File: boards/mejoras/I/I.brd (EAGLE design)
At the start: 100 x 45 mm, 5 parts

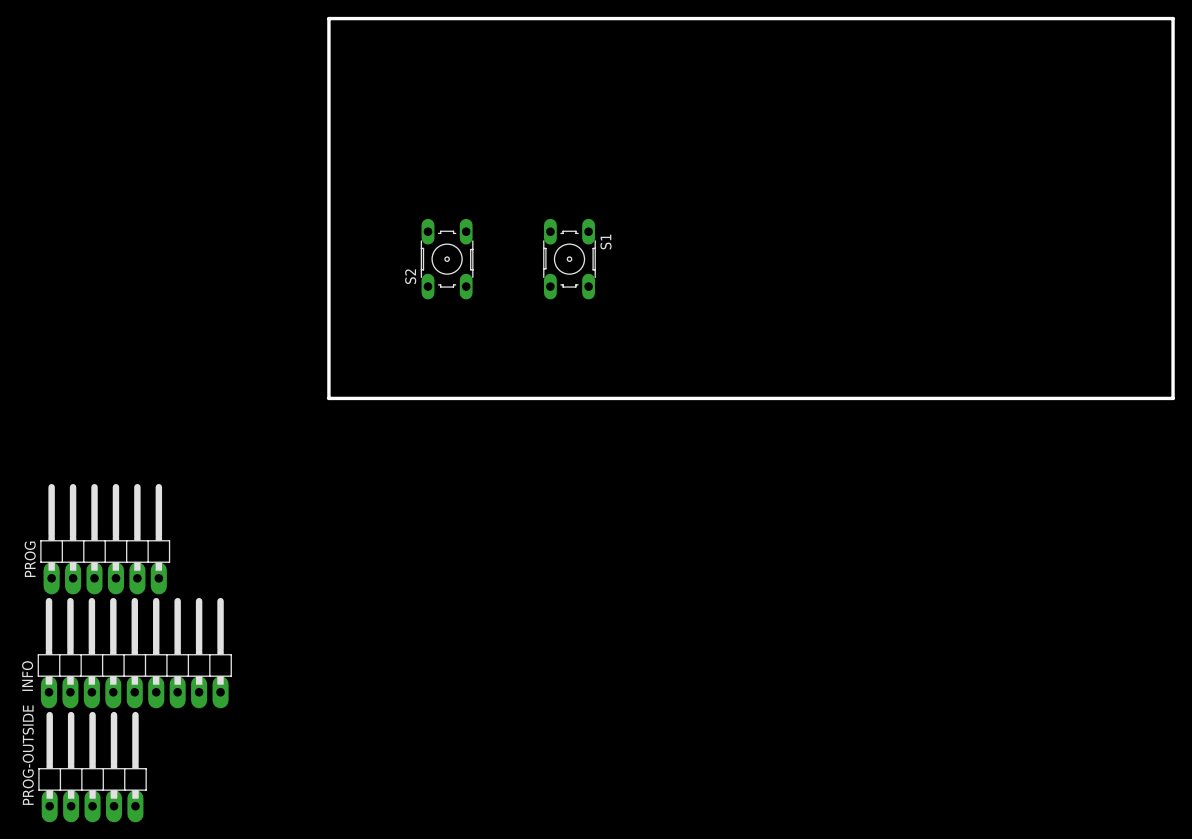
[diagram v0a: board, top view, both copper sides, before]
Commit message: added circuit H and I
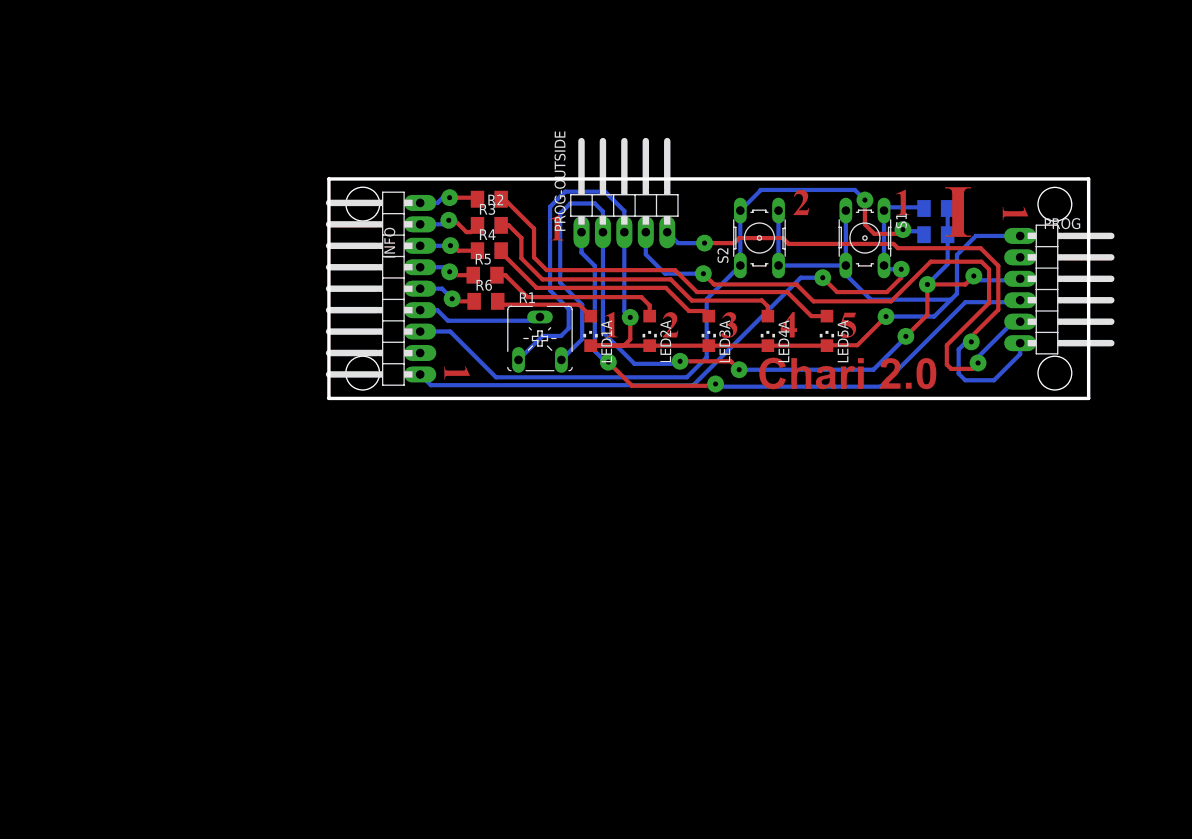
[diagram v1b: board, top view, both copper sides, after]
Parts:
- added LED1A, LED2A, LED3A, LED4A, LED5A: (no value), adafruit:CHIPLED_1206
- added R1: (no value), pot:CA6V
- added R2, R3, R4, R5, R6, R7, R8: (no value), rcl:M1206
- moved PROG 116.2 mm to (85.7, 12.9), turned to 270 degrees
- moved PROG-OUTSIDE 92.7 mm to (35.0, 23.5)
- moved INFO 53.3 mm to (7.00, 13.0), turned to 90 degrees
- moved S2 37.1 mm to (51.0, 19.0)
- moved S1 35.1 mm to (63.5, 19.0)
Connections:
- new net 5V: PROG-OUTSIDE.2, PROG.3, R1.E, R7.2, R8.2
- new net MCRL: PROG-OUTSIDE.1, PROG.4
- new net N$1: LED1A.A, R6.2
- new net N$10: INFO.5, R6.1
- new net N$11: INFO.4, R1.S
- new net N$2: LED2A.A, R5.2
- new net N$3: LED3A.A, R4.2
- new net N$4: LED4A.A, R3.2
- new net N$5: LED5A.A, R2.2
- new net N$6: INFO.9, R2.1
- new net N$7: INFO.8, R3.1
- new net N$8: INFO.7, R4.1
- new net N$9: INFO.6, R5.1
- new net PGC: PROG-OUTSIDE.5, PROG.6
- new net PGD: PROG-OUTSIDE.4, PROG.5
- net B1: now also INFO.1, R7.1
- net B2: now also INFO.3, R8.1
- net GND: now also LED1A.C, LED2A.C, LED3A.C, LED4A.C, LED5A.C, PROG-OUTSIDE.3, PROG.1, R1.A
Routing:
- net GND: track 0.00 -> 148.6 mm, vias 0 -> 2
- net 5V: track 0.00 -> 108.9 mm, vias 0 -> 5
- net B2: track 0.00 -> 83.3 mm, vias 0 -> 2
- net B1: track 0.00 -> 79.0 mm, vias 0 -> 2
- net PGD: track 0.00 -> 72.9 mm, vias 0 -> 2
- net MCRL: track 0.00 -> 71.5 mm, vias 0 -> 2
- net PGC: track 0.00 -> 66.6 mm, vias 0 -> 2
- net N$5: track 0.00 -> 46.3 mm
- net N$4: track 0.00 -> 38.8 mm
- net N$3: track 0.00 -> 27.9 mm
- net N$2: track 0.00 -> 20.8 mm
- net N$11: track 0.00 -> 14.9 mm
- net N$1: track 0.00 -> 11.7 mm
- net N$7: track 0.00 -> 7.90 mm, vias 0 -> 1
- net N$6: track 0.00 -> 7.85 mm, vias 0 -> 1
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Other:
- board size 100 x 45 mm -> 90 x 26 mm

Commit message: updated board h and i
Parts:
- moved R2 20.3 mm to (37.9, 16.2)
- moved R8 15.0 mm to (57.3, 23.0)
- moved R3 14.8 mm to (32.8, 15.2)
- moved R4 9.38 mm to (27.7, 14.0)
- moved PROG 6.00 mm to (79.7, 12.9)
- moved R5 3.18 mm to (21.6, 15.3)
- moved R6 3.13 mm to (21.6, 12.4)
- moved INFO 3.00 mm to (10.0, 13.0)
- moved R7 2.11 mm to (69.8, 22.3)
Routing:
- net N$5: track 46.3 -> 22.4 mm
- net N$6: track 7.85 -> 28.5 mm
- net B2: track 83.3 -> 62.9 mm, vias 2 -> 0
- net N$4: track 38.8 -> 21.4 mm
- net N$7: track 7.90 -> 21.4 mm
- net PGC: track 66.6 -> 53.2 mm
- net 5V: track 108.9 -> 122.2 mm, vias 5 -> 4
- net PGD: track 72.9 -> 62.3 mm
- net GND: track 148.6 -> 138.1 mm
- net N$3: track 27.9 -> 17.7 mm
- net B1: track 79.0 -> 69.1 mm
- net N$8: track 7.05 -> 14.9 mm
- net MCRL: track 71.5 -> 66.4 mm
- net N$11: track 14.9 -> 11.6 mm
- net N$1: track 11.7 -> 9.10 mm
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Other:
- board size 90 x 26 mm -> 80 x 26 mm

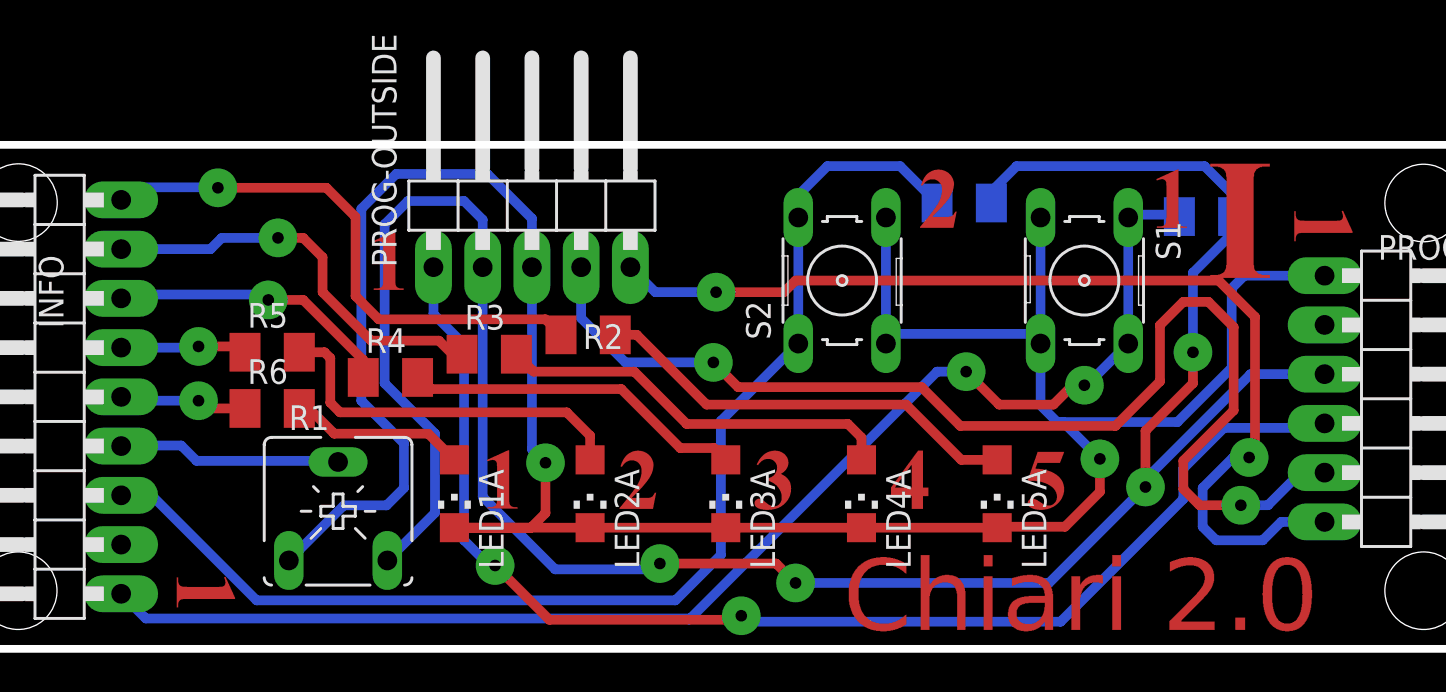
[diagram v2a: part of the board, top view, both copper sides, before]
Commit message: added on button
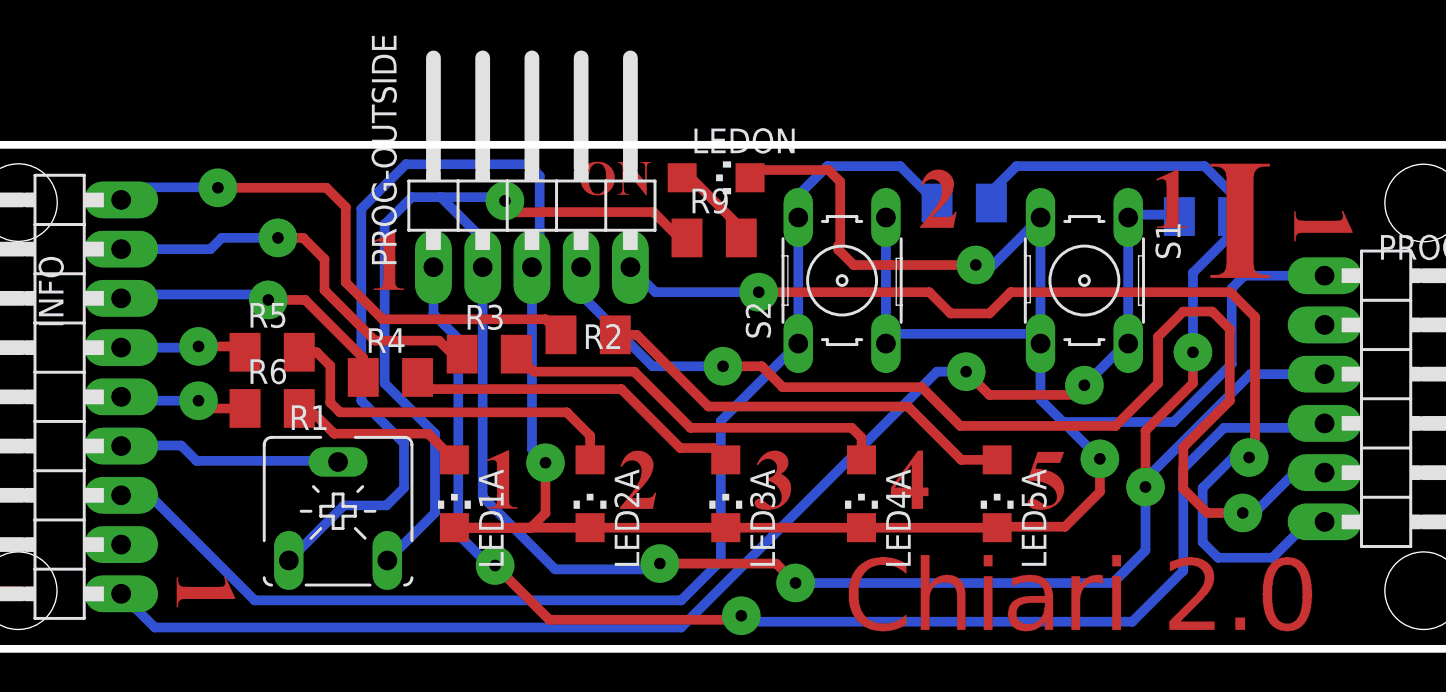
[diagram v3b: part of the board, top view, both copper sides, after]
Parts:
- added LEDON: (no value), adafruit:CHIPLED_1206
- added R9: (no value), rcl:M1206
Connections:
- new net N$12: LEDON.A, R9.2
- net 5V: now also R9.1
- net GND: now also LEDON.C
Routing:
- net GND: track 138.1 -> 160.5 mm, vias 2 -> 3
- net 5V: track 122.2 -> 138.9 mm, vias 4 -> 5
- net N$12: track 0.00 -> 4.63 mm
- net MCRL: track 66.4 -> 68.6 mm
- net PGC: track 53.2 -> 54.8 mm
- net PGD: track 62.3 -> 60.9 mm
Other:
- board text added: "C:/Users/Ariel/GitHub/Sumo-Robot-Programs-Database/boards/mejoras/I/ON.bmp"

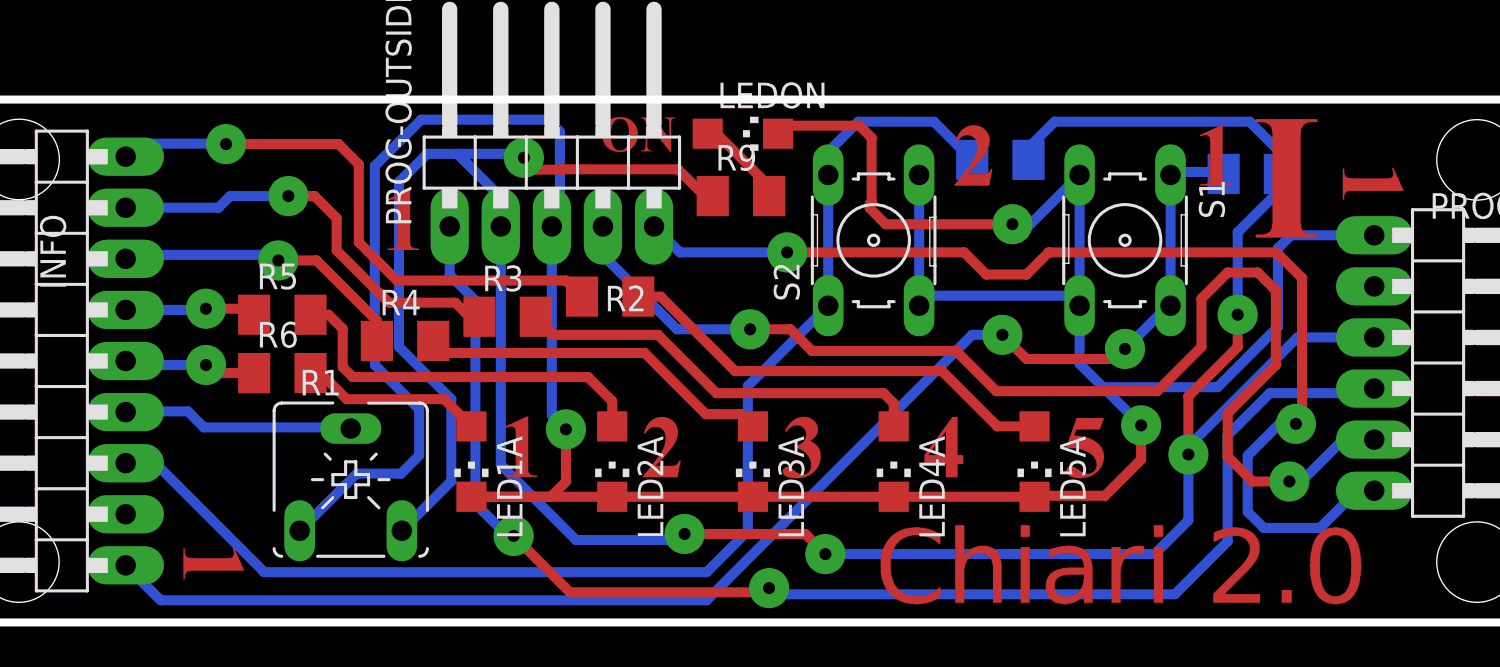
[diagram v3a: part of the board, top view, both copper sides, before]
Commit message: small fixes to g and i
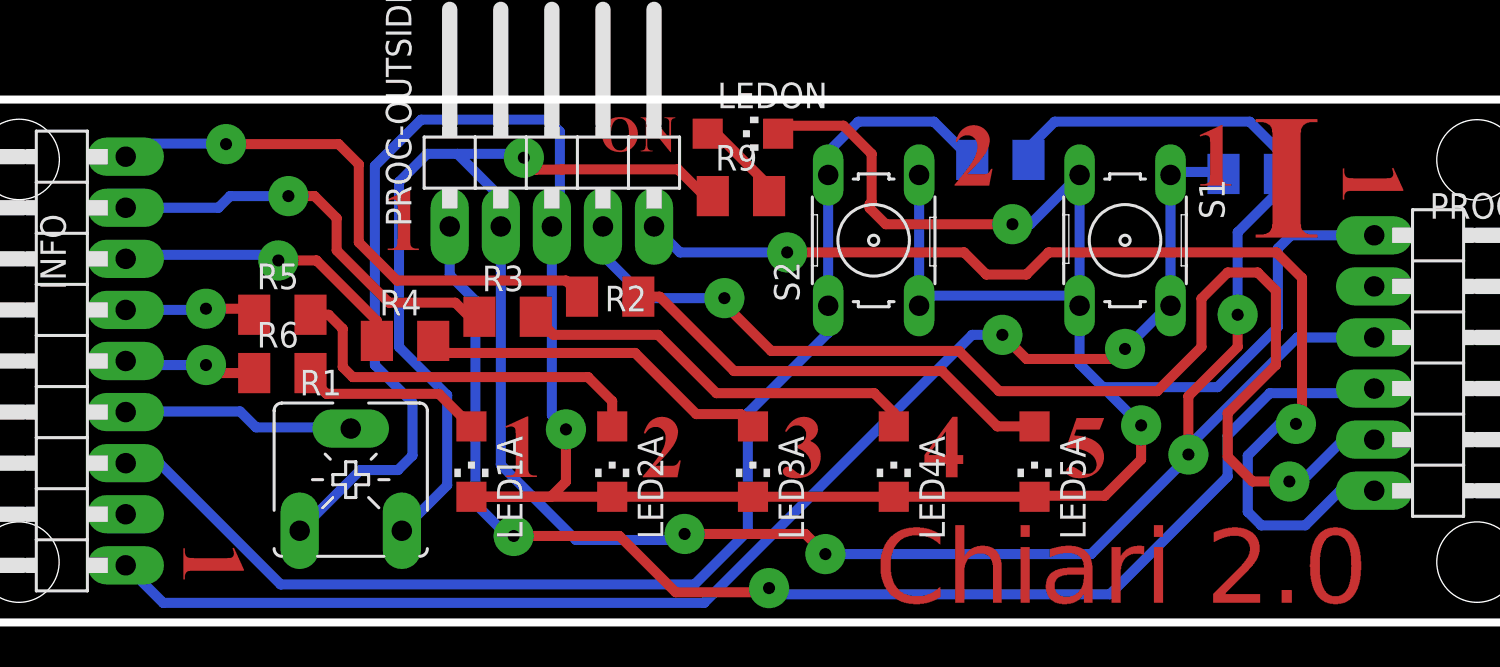
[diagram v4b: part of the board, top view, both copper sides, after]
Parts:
- R1: device pot:CA6V -> pot-enhanced:CA6V
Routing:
- net 5V: track 138.9 -> 136.9 mm
- net MCRL: track 68.6 -> 66.7 mm
- net GND: track 160.5 -> 159.5 mm
- net B2: track 63.1 -> 63.6 mm
